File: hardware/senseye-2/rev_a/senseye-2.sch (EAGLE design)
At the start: 15 parts, among them U1 ADC121S101, U2 ADC121S101, U3 ADC121S101

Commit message: added power header
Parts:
- added JP4: (no value), SparkFun-Connectors:M02PTH
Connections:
- net !CS0: now also U1.!CS; no longer U2.!CS
- net !CS1: now also U2.!CS; no longer U1.!CS
- net ANALOG0: now also U1.VIN; no longer U2.VIN
- net GND: now also JP4.2
- net N$1: now also U2.VIN; no longer U1.VIN
- net VCC: now also JP4.1
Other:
- moved on the sheet: U1, U2
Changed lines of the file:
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@@
 <attribute name="AUTHOR" value="Neal Jackson"/>
 <attribute name="REV" value="A"/>
-<attribute name="TITLE" value="Senseye"/>
+<attribute name="TITLE" value="SensEye-2"/>
 </attributes>
 <variantdefs>
@@
 </classes>
 <parts>
-<part name="FRAME1" library="frames" deviceset="LETTER_L" device=""/>
+<part name="U2" library="chips" deviceset="ADC121S101" device=""/>
 <part name="U1" library="chips" deviceset="ADC121S101" device=""/>
-<part name="U2" library="chips" deviceset="ADC121S101" device=""/>
 <part name="JP2" library="senseye" deviceset="STONYMAN" device=""/>
 <part name="JP1" library="senseye" deviceset="STONYMAN" device=""/>
@@
 <part name="U3" library="chips" deviceset="ADC121S101" device=""/>
 <part name="R3" library="passives" deviceset="RESISTOR" device="0402_RES" value="10k"/>
+<part name="JP4" library="SparkFun-Connectors" deviceset="M02" device="PTH"/>
+<part name="FRAME1" library="frames" deviceset="LETTER_L" device=""/>
 </parts>
 <sheets>
@@
 </plain>
 <instances>
-<instance part="FRAME1" gate="G$1" x="0" y="0"/>
-<instance part="FRAME1" gate="G$2" x="147.32" y="0"/>
-<instance part="U1" gate="G$1" x="114.3" y="114.3"/>
-<instance part="U2" gate="G$1" x="114.3" y="152.4"/>
+<instance part="U2" gate="G$1" x="114.3" y="114.3"/>
+<instance part="U1" gate="G$1" x="114.3" y="152.4"/>
 <instance part="JP2" gate="G$1" x="2.54" y="111.76"/>
 <instance part="JP1" gate="G$1" x="2.54" y="149.86"/>
@@
 <instance part="U3" gate="G$1" x="114.3" y="76.2"/>
 <instance part="R3" gate="G$1" x="106.68" y="71.12" rot="R270"/>
+<instance part="JP4" gate="G$1" x="5.08" y="55.88"/>
+<instance part="FRAME1" gate="G$1" x="0" y="0"/>
+<instance part="FRAME1" gate="G$2" x="147.32" y="0"/>
 </instances>
 <busses>
@@
 </segment>
 <segment>
-<pinref part="U2" gate="G$1" pin="GND"/>
+<pinref part="U1" gate="G$1" pin="GND"/>
 <wire x1="109.22" y1="160.02" x2="106.68" y2="160.02" width="0.1524" layer="91"/>
 <label x="106.68" y="160.02" size="1.27" layer="95" rot="R180" xref="yes"/>
@@
 </segment>
 <segment>
-<pinref part="U1" gate="G$1" pin="GND"/>
+<pinref part="U2" gate="G$1" pin="GND"/>
 <wire x1="109.22" y1="121.92" x2="106.68" y2="121.92" width="0.1524" layer="91"/>
 <label x="106.68" y="121.92" size="1.27" layer="95" rot="R180" xref="yes"/>
@@
 <label x="226.06" y="170.18" size="1.27" layer="95" rot="MR0" xref="yes"/>
 </segment>
+<segment>
+<pinref part="JP4" gate="G$1" pin="2"/>
+<wire x1="12.7" y1="58.42" x2="15.24" y2="58.42" width="0.1524" layer="91"/>
+<label x="15.24" y="58.42" size="1.27" layer="95" xref="yes"/>
+</segment>
 </net>
 <net name="VCC" class="0">
@@
 </segment>
 <segment>
-<pinref part="U2" gate="G$1" pin="VA"/>
+<pinref part="U1" gate="G$1" pin="VA"/>
 <wire x1="109.22" y1="165.1" x2="106.68" y2="165.1" width="0.1524" layer="91"/>
 <label x="106.68" y="165.1" size="1.27" layer="95" rot="R180" xref="yes"/>
@@
 </segment>
 <segment>
-<pinref part="U1" gate="G$1" pin="VA"/>
+<pinref part="U2" gate="G$1" pin="VA"/>
 <wire x1="109.22" y1="127" x2="106.68" y2="127" width="0.1524" layer="91"/>
 <label x="106.68" y="127" size="1.27" layer="95" rot="R180" xref="yes"/>
@@
 <label x="226.06" y="167.64" size="1.27" layer="95" rot="MR0" xref="yes"/>
 </segment>
+<segment>
+<pinref part="JP4" gate="G$1" pin="1"/>
+<wire x1="12.7" y1="55.88" x2="15.24" y2="55.88" width="0.1524" layer="91"/>
+<label x="15.24" y="55.88" size="1.27" layer="95" xref="yes"/>
+</segment>
 </net>
 <net name="RESP0" class="0">
@@
 <segment>
 <pinref part="JP1" gate="G$1" pin="ANALOG"/>
-<pinref part="U2" gate="G$1" pin="VIN"/>
+<pinref part="U1" gate="G$1" pin="VIN"/>
 <wire x1="25.4" y1="154.94" x2="106.68" y2="154.94" width="0.1524" layer="91"/>
 <pinref part="R1" gate="G$1" pin="1"/>
@@
 <net name="!CS0" class="0">
 <segment>
-<pinref part="U2" gate="G$1" pin="!CS"/>
+<pinref part="U1" gate="G$1" pin="!CS"/>
 <wire x1="137.16" y1="165.1" x2="152.4" y2="165.1" width="0.1524" layer="91"/>
 <pinref part="JP6" gate="G$1" pin="15"/>
@@
 <net name="!CS1" class="0">
 <segment>
-<pinref part="U1" gate="G$1" pin="!CS"/>
+<pinref part="U2" gate="G$1" pin="!CS"/>
 <wire x1="152.4" y1="127" x2="137.16" y2="127" width="0.1524" layer="91"/>
 <pinref part="U3" gate="G$1" pin="!CS"/>
@@
 <net name="SCLK" class="0">
 <segment>
-<pinref part="U1" gate="G$1" pin="SCLK"/>
+<pinref part="U2" gate="G$1" pin="SCLK"/>
 <wire x1="137.16" y1="116.84" x2="147.32" y2="116.84" width="0.1524" layer="91"/>
 <wire x1="147.32" y1="116.84" x2="157.48" y2="116.84" width="0.1524" layer="91"/>
 <wire x1="157.48" y1="116.84" x2="157.48" y2="127" width="0.1524" layer="91"/>
-<pinref part="U2" gate="G$1" pin="SCLK"/>
+<pinref part="U1" gate="G$1" pin="SCLK"/>
 <wire x1="137.16" y1="154.94" x2="147.32" y2="154.94" width="0.1524" layer="91"/>
 <wire x1="147.32" y1="154.94" x2="147.32" y2="116.84" width="0.1524" layer="91"/>
@@
 <net name="SDATA" class="0">
 <segment>
+<pinref part="U1" gate="G$1" pin="SDATA"/>
 <pinref part="U2" gate="G$1" pin="SDATA"/>
-<pinref part="U1" gate="G$1" pin="SDATA"/>
 <wire x1="137.16" y1="121.92" x2="149.86" y2="121.92" width="0.1524" layer="91"/>
 <wire x1="149.86" y1="121.92" x2="154.94" y2="121.92" width="0.1524" layer="91"/>
@@
 <net name="N$1" class="0">
 <segment>
-<pinref part="U1" gate="G$1" pin="VIN"/>
+<pinref part="U2" gate="G$1" pin="VIN"/>
 <wire x1="109.22" y1="116.84" x2="106.68" y2="116.84" width="0.1524" layer="91"/>
 <pinref part="R2" gate="G$1" pin="1"/>

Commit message: using spi instead of i2c
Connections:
- removed net !CS1: JP6.16, U2.!CS, U3.!CS
- removed net SCLK: JP6.18, U1.SCLK, U2.SCLK, U3.SCLK
- removed net SDATA: JP6.17, U1.SDATA, U2.SDATA, U3.SDATA
- new net N$6: JP6.18, U2.!CS, U3.!CS
- new net SCLK0: JP6.17, U1.SCLK
- new net SCLK1: JP6.20, U2.SCLK, U3.SCLK
- new net SDATA0: JP6.16, U1.SDATA
- new net SDATA1: JP6.19, U2.SDATA, U3.SDATA
- net LED: now also JP6.22; no longer JP6.19
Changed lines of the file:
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@@
 </segment>
 </net>
-<net name="!CS1" class="0">
-<segment>
-<pinref part="U2" gate="G$1" pin="!CS"/>
-<wire x1="152.4" y1="127" x2="137.16" y2="127" width="0.1524" layer="91"/>
-<pinref part="U3" gate="G$1" pin="!CS"/>
-<wire x1="137.16" y1="88.9" x2="152.4" y2="88.9" width="0.1524" layer="91"/>
-<wire x1="152.4" y1="88.9" x2="152.4" y2="127" width="0.1524" layer="91"/>
-<junction x="152.4" y="127"/>
-<pinref part="JP6" gate="G$1" pin="16"/>
-<wire x1="152.4" y1="127" x2="152.4" y2="132.08" width="0.1524" layer="91"/>
-<wire x1="152.4" y1="132.08" x2="231.14" y2="132.08" width="0.1524" layer="91"/>
-</segment>
-</net>
-<net name="SCLK" class="0">
+<net name="SCLK1" class="0">
 <segment>
 <pinref part="U2" gate="G$1" pin="SCLK"/>
-<wire x1="137.16" y1="116.84" x2="147.32" y2="116.84" width="0.1524" layer="91"/>
-<wire x1="147.32" y1="116.84" x2="157.48" y2="116.84" width="0.1524" layer="91"/>
-<wire x1="157.48" y1="116.84" x2="157.48" y2="127" width="0.1524" layer="91"/>
-<pinref part="U1" gate="G$1" pin="SCLK"/>
-<wire x1="137.16" y1="154.94" x2="147.32" y2="154.94" width="0.1524" layer="91"/>
-<wire x1="147.32" y1="154.94" x2="147.32" y2="116.84" width="0.1524" layer="91"/>
-<junction x="147.32" y="116.84"/>
+<wire x1="137.16" y1="116.84" x2="157.48" y2="116.84" width="0.1524" layer="91"/>
 <pinref part="U3" gate="G$1" pin="SCLK"/>
 <wire x1="137.16" y1="78.74" x2="157.48" y2="78.74" width="0.1524" layer="91"/>
 <wire x1="157.48" y1="78.74" x2="157.48" y2="116.84" width="0.1524" layer="91"/>
+<pinref part="JP6" gate="G$1" pin="20"/>
+<wire x1="157.48" y1="116.84" x2="157.48" y2="121.92" width="0.1524" layer="91"/>
+<wire x1="157.48" y1="121.92" x2="231.14" y2="121.92" width="0.1524" layer="91"/>
 <junction x="157.48" y="116.84"/>
-<pinref part="JP6" gate="G$1" pin="18"/>
-<wire x1="157.48" y1="127" x2="231.14" y2="127" width="0.1524" layer="91"/>
 </segment>
 </net>
-<net name="SDATA" class="0">
+<net name="SDATA1" class="0">
 <segment>
-<pinref part="U1" gate="G$1" pin="SDATA"/>
 <pinref part="U2" gate="G$1" pin="SDATA"/>
-<wire x1="137.16" y1="121.92" x2="149.86" y2="121.92" width="0.1524" layer="91"/>
-<wire x1="149.86" y1="121.92" x2="154.94" y2="121.92" width="0.1524" layer="91"/>
-<wire x1="154.94" y1="121.92" x2="154.94" y2="129.54" width="0.1524" layer="91"/>
-<wire x1="137.16" y1="160.02" x2="149.86" y2="160.02" width="0.1524" layer="91"/>
-<wire x1="149.86" y1="160.02" x2="149.86" y2="121.92" width="0.1524" layer="91"/>
-<junction x="149.86" y="121.92"/>
+<wire x1="137.16" y1="121.92" x2="154.94" y2="121.92" width="0.1524" layer="91"/>
 <pinref part="U3" gate="G$1" pin="SDATA"/>
 <wire x1="137.16" y1="83.82" x2="154.94" y2="83.82" width="0.1524" layer="91"/>
 <wire x1="154.94" y1="83.82" x2="154.94" y2="121.92" width="0.1524" layer="91"/>
+<wire x1="154.94" y1="121.92" x2="154.94" y2="124.46" width="0.1524" layer="91"/>
+<pinref part="JP6" gate="G$1" pin="19"/>
+<wire x1="154.94" y1="124.46" x2="231.14" y2="124.46" width="0.1524" layer="91"/>
 <junction x="154.94" y="121.92"/>
-<pinref part="JP6" gate="G$1" pin="17"/>
-<wire x1="154.94" y1="129.54" x2="231.14" y2="129.54" width="0.1524" layer="91"/>
 </segment>
 </net>
@@
 <wire x1="220.98" y1="106.68" x2="220.98" y2="101.6" width="0.1524" layer="91"/>
 <wire x1="220.98" y1="101.6" x2="218.44" y2="101.6" width="0.1524" layer="91"/>
-<pinref part="JP6" gate="G$1" pin="19"/>
-<wire x1="220.98" y1="106.68" x2="220.98" y2="124.46" width="0.1524" layer="91"/>
-<wire x1="220.98" y1="124.46" x2="231.14" y2="124.46" width="0.1524" layer="91"/>
+<wire x1="220.98" y1="106.68" x2="220.98" y2="116.84" width="0.1524" layer="91"/>
+<pinref part="JP6" gate="G$1" pin="22"/>
+<wire x1="220.98" y1="116.84" x2="231.14" y2="116.84" width="0.1524" layer="91"/>
 </segment>
 </net>
+<net name="SCLK0" class="0">
+<segment>
+<pinref part="U1" gate="G$1" pin="SCLK"/>
+<wire x1="137.16" y1="154.94" x2="147.32" y2="154.94" width="0.1524" layer="91"/>
+<wire x1="147.32" y1="154.94" x2="147.32" y2="129.54" width="0.1524" layer="91"/>
+<pinref part="JP6" gate="G$1" pin="17"/>
+<wire x1="147.32" y1="129.54" x2="231.14" y2="129.54" width="0.1524" layer="91"/>
+</segment>
+</net>
+<net name="N$6" class="0">
+<segment>
+<pinref part="U2" gate="G$1" pin="!CS"/>
+<pinref part="U3" gate="G$1" pin="!CS"/>
+<wire x1="137.16" y1="88.9" x2="152.4" y2="88.9" width="0.1524" layer="91"/>
+<wire x1="152.4" y1="88.9" x2="152.4" y2="127" width="0.1524" layer="91"/>
+<wire x1="152.4" y1="127" x2="137.16" y2="127" width="0.1524" layer="91"/>
+<pinref part="JP6" gate="G$1" pin="18"/>
+<wire x1="152.4" y1="127" x2="231.14" y2="127" width="0.1524" layer="91"/>
+<junction x="152.4" y="127"/>
+</segment>
+</net>
+<net name="SDATA0" class="0">
+<segment>
+<pinref part="JP6" gate="G$1" pin="16"/>
+<wire x1="231.14" y1="132.08" x2="149.86" y2="132.08" width="0.1524" layer="91"/>
+<wire x1="149.86" y1="132.08" x2="149.86" y2="160.02" width="0.1524" layer="91"/>
+<pinref part="U1" gate="G$1" pin="SDATA"/>
+<wire x1="149.86" y1="160.02" x2="137.16" y2="160.02" width="0.1524" layer="91"/>
+</segment>
+</net>

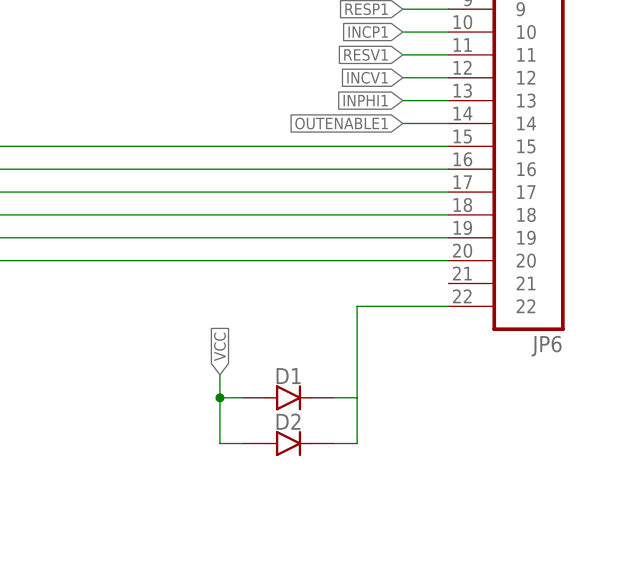
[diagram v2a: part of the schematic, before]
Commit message: added drills for hinges
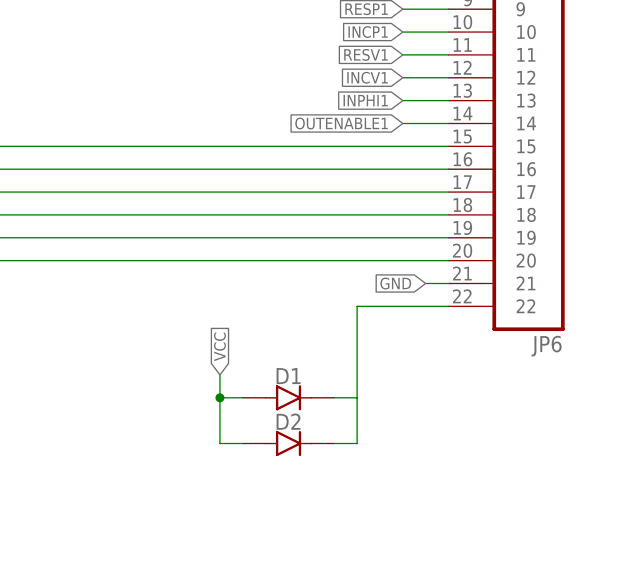
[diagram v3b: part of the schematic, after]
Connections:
- net GND: now also JP6.21
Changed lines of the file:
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@@
 <label x="15.24" y="58.42" size="1.27" layer="95" xref="yes"/>
+</segment>
+<segment>
+<pinref part="JP6" gate="G$1" pin="21"/>
+<wire x1="231.14" y1="119.38" x2="228.6" y2="119.38" width="0.1524" layer="91"/>
+<label x="228.6" y="119.38" size="1.27" layer="95" rot="R180" xref="yes"/>
 </segment>
 </net>

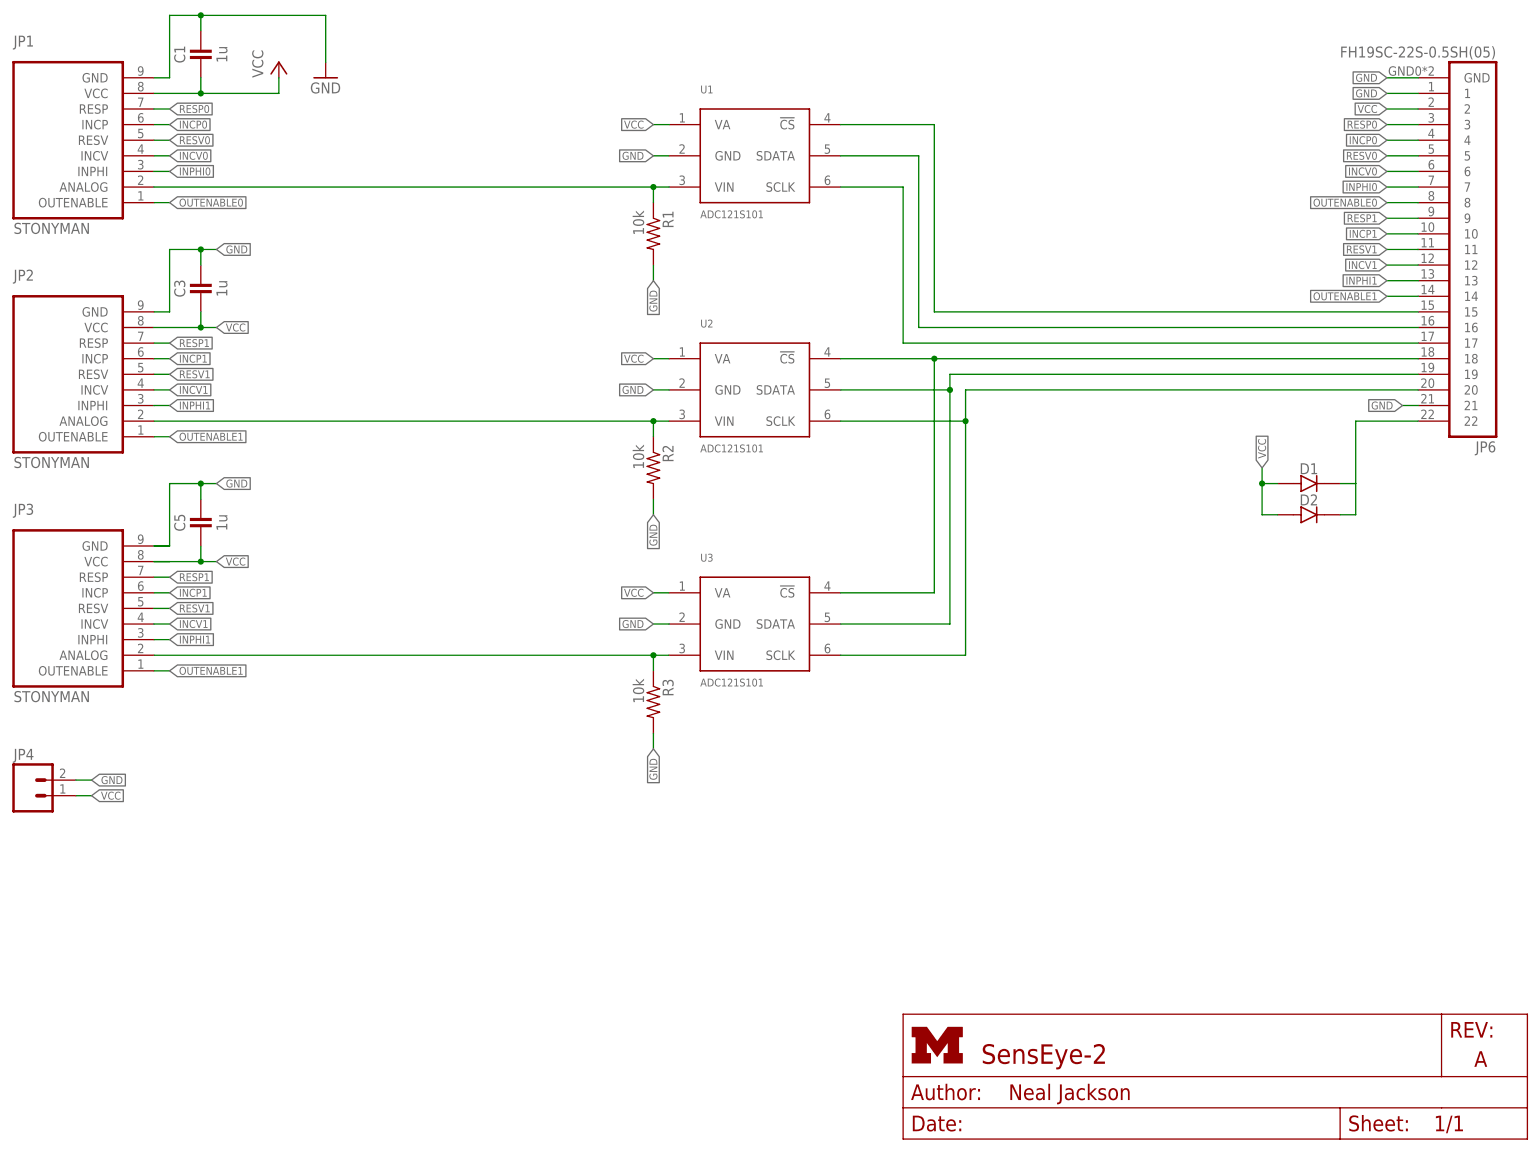
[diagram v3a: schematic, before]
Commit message: added inline resistors for diodes
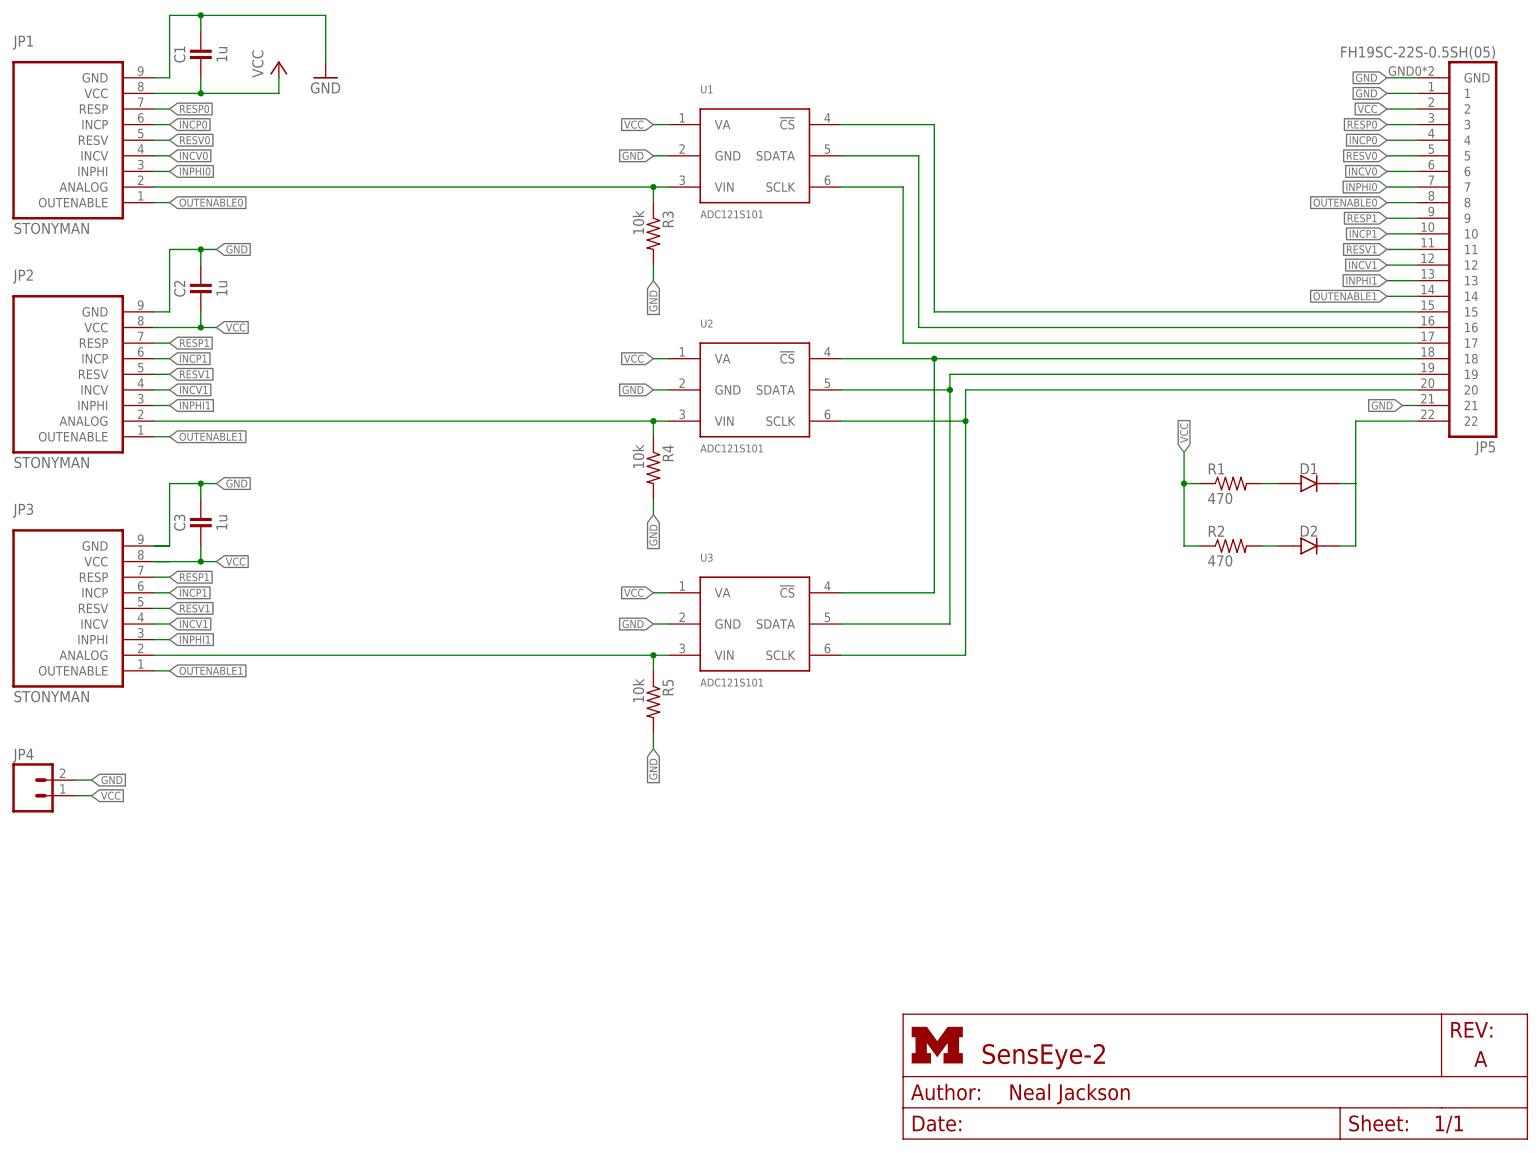
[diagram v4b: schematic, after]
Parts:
- removed C5: 1u, passives:CAPACITOR
- added C2: 1u, passives:CAPACITOR
- added R4, R5: 10k, passives:RESISTOR0402_RES
- R1, R2: value 10k -> 470
- renumbered JP6 to JP5
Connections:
- new net N$2: D1.ANODE, R1.2
- new net N$5: D2.ANODE, R2.2
- net ANALOG0: now also R3.1; no longer R1.1
- net GND: now also C2.1, R4.2, R5.2; no longer C5.1, R1.2, R2.2
- net N$1: now also R4.1; no longer R2.1
- net N$3: now also R5.1; no longer R3.1
- net VCC: now also C2.2, R1.1, R2.1; no longer C5.2, D1.ANODE, D2.ANODE
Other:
- moved on the sheet: C3, D2, R1, R2, R3
